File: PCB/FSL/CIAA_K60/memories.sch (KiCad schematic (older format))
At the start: 28 parts, among them J1001 SD CARD, Q1001 FDN340P, U1001 S25FL032P0XMFI013, U1002 24AA1025, U1003 24AA025E48

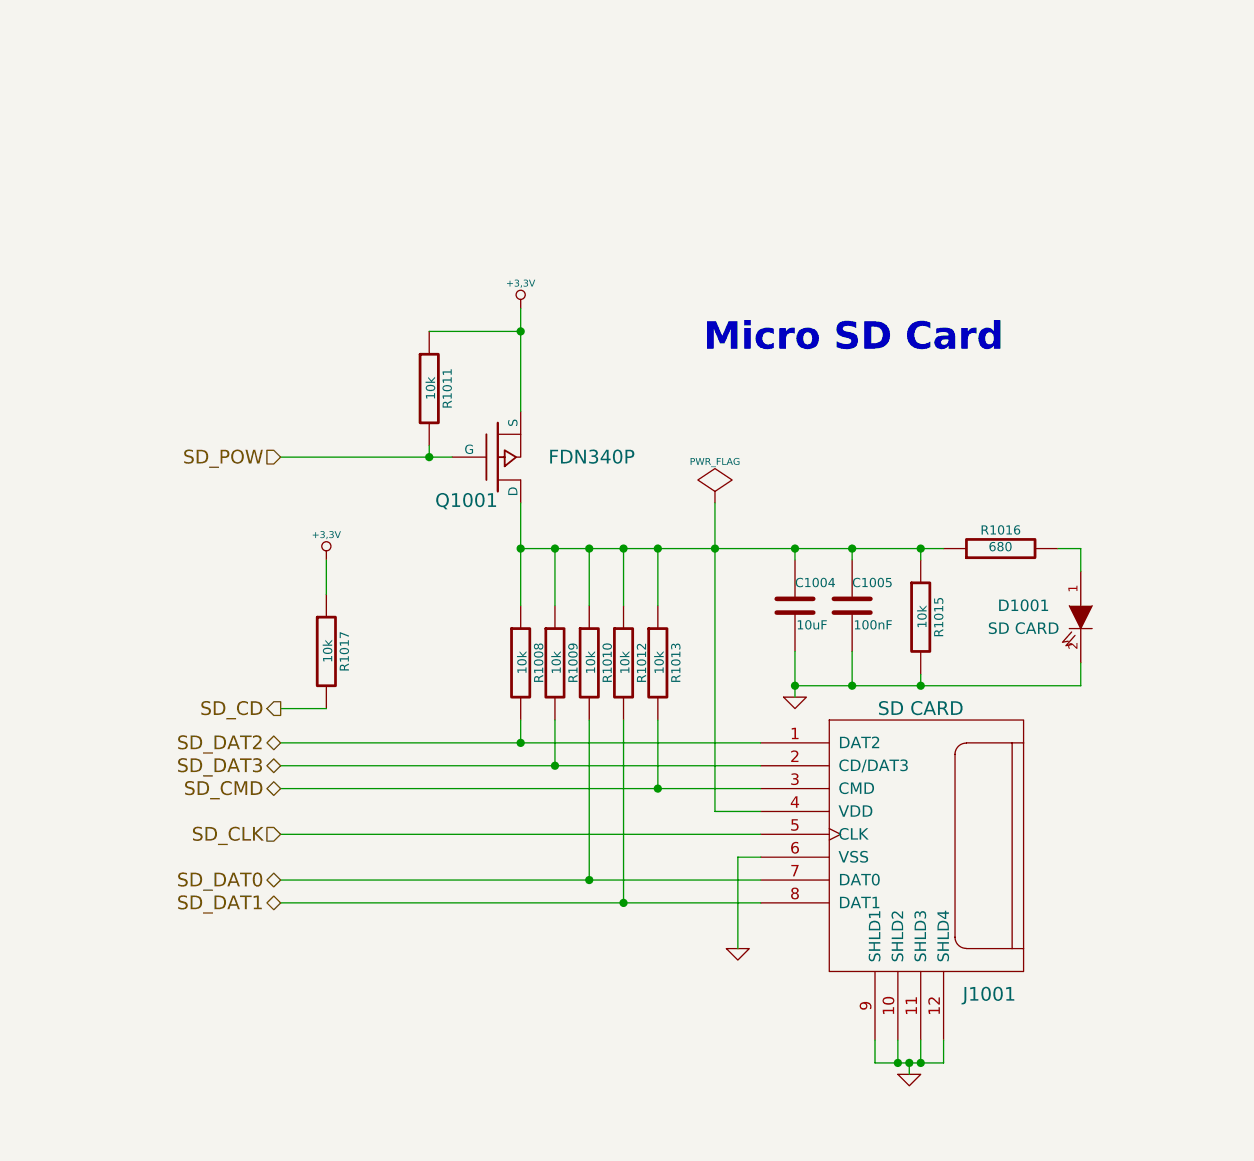
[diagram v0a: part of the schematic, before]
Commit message: Actualizacion de esquematicos. Circuito impreso y modelos 3D
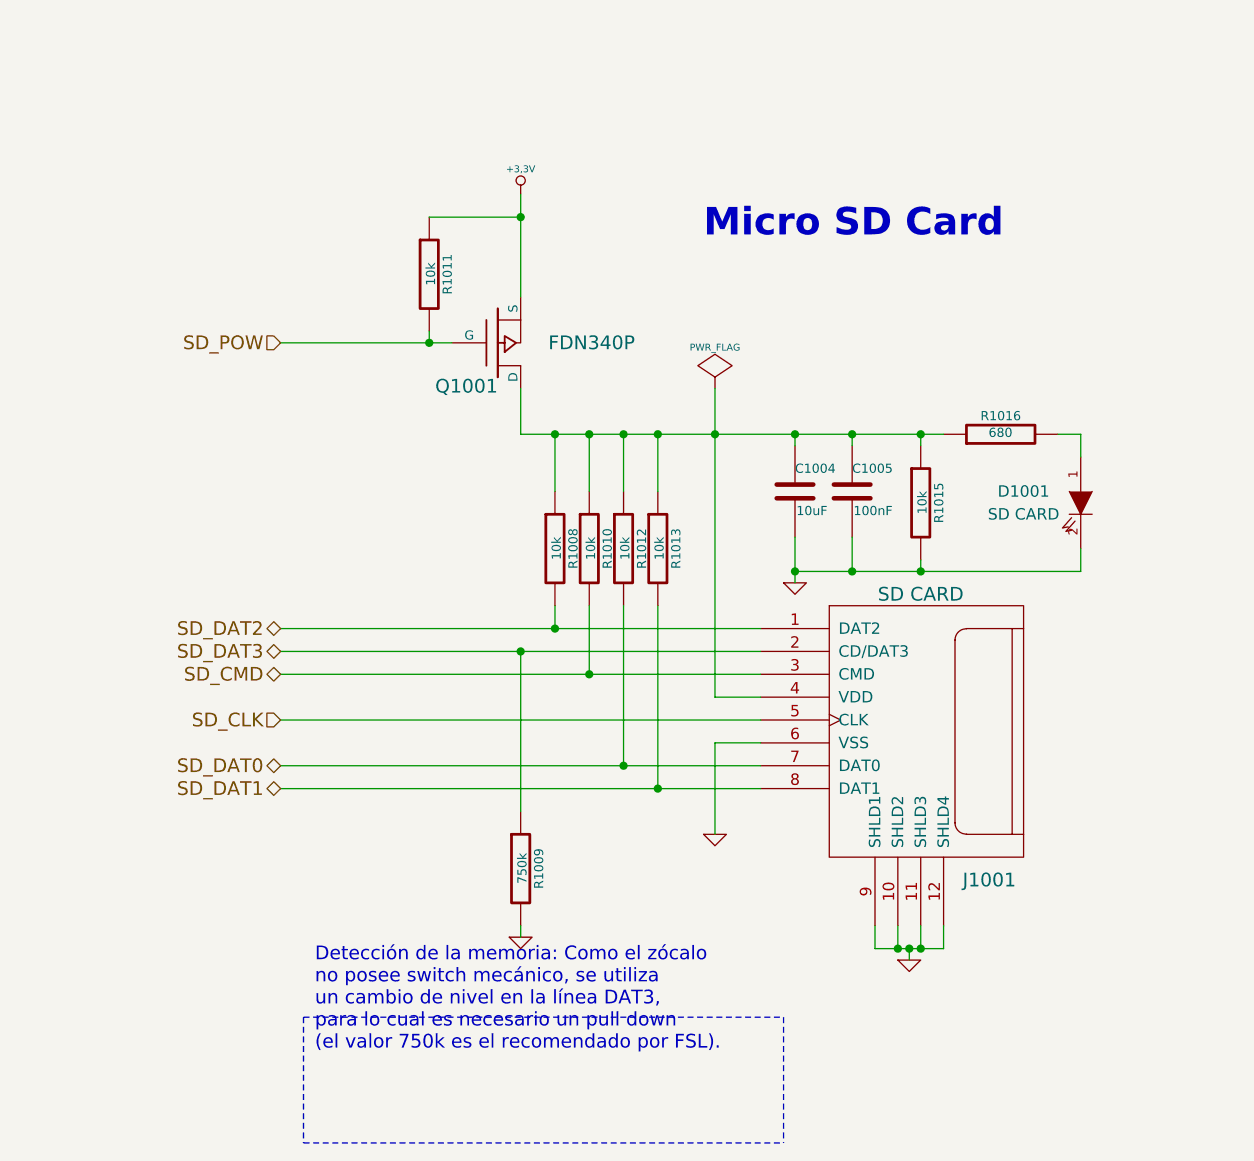
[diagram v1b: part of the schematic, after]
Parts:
- removed R1017: 10k, r_0603, symbol R
- R1009: value 10k -> 750k; Descripcion RES 10K OHM 1/10W 5% 0603 SMD -> RES 750K OHM 1/10W 5% 0603 SMD; Digikey/Mouser 311-10KGRCT-ND -> 311-750KGRCT-ND; Nro. parte RC0603JR-0710KL -> RC0603JR-07750KL
- U1001: footprint SOIC-8 -> SOIC-8_WIDE; Footprint estandar 8-SOIC -> SOIC-8 WIDE
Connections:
- net GND: now also R1009.2
- net SD_CMD: now also R1010.2; no longer R1013.2
- net SD_DAT0: now also R1012.2; no longer R1010.2
- net SD_DAT1: now also R1013.2; no longer R1012.2
- net SD_DAT3: now also R1009.1; no longer R1009.2
- net at C1004.1, C1005.1, J1001.4 (VDD)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: no longer R1009.1
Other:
- note added: "Detección de la memoria: Como el zócalo \nno posee switch mecánico, se utiliza \nun cambio de nivel en la línea DAT3,\npara lo cual es necesario un pull down\n(el valor 750k es el recomendado por FSL)."
- moved on the sheet: C1004, C1005, D1001, J1001, Q1001, R1008, R1010, R1011, R1012, R1013, R1015, R1016

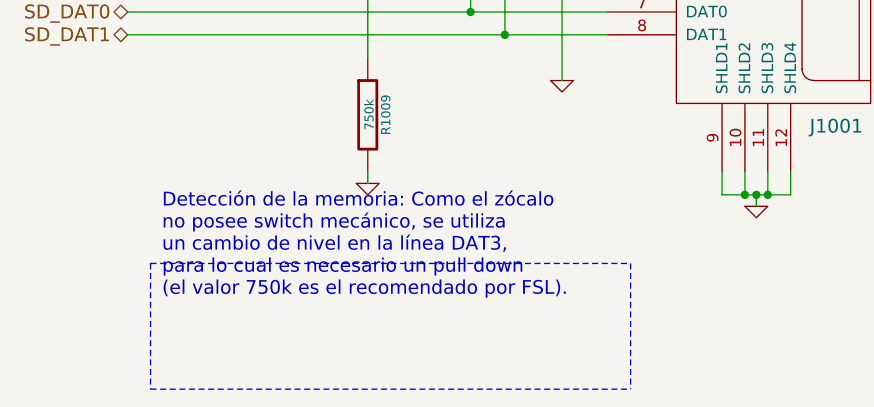
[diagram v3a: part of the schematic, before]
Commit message: Sch files adapted to new eeschema. Fixing some text locations.
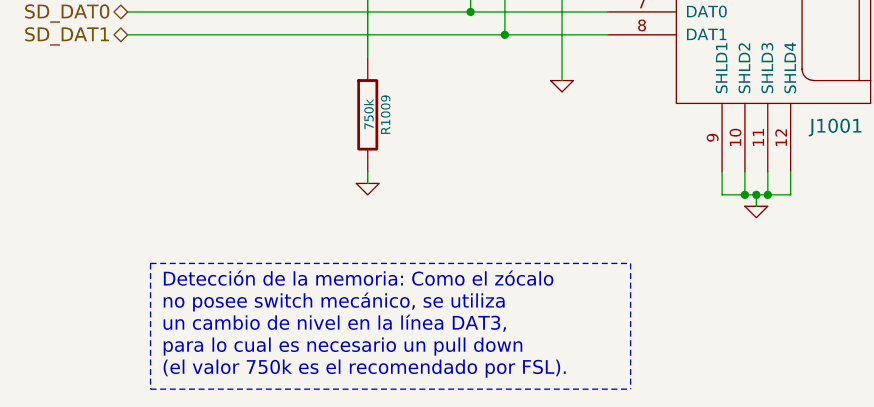
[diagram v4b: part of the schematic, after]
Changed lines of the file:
@@
 EESchema Schematic File Version 2
 LIBS:CIAAK60LIB
-EELAYER 27 0
+LIBS:CIAA_K60-cache
+EELAYER 25 0
 EELAYER END
 $Descr A4 11693 8268
@@
 	1    0    0    -1
 $EndComp
-Text Notes 2000 7250 0    60   ~ 0
+Text Notes 2000 7600 0    60   ~ 0
 Detección de la memoria: Como el zócalo \nno posee switch mecánico, se utiliza \nun cambio de nivel en la línea DAT3,\npara lo cual es necesario un pull down\n(el valor 750k es el recomendado por FSL).
 $Comp

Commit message: Renaming symbol field-names in .sch files for KiCost integration.
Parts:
- C1001, C1002, C1003, C1005: Desc (none) -> CAP CER 0,1UF 16V 10% X7R 0603; Descripcion CAP CER 0,1UF 16V 10% X7R 0603 -> (none); Digikey# (none) -> 399-1096-1-ND; Digikey/Mouser 399-1096-1-ND -> (none); Fabricante Kemet -> (none); Manf (none) -> Kemet; Manf# (none) -> C0603C104K4RACTU; Nro. parte C0603C104K4RACTU -> (none)
- C1004: Desc (none) -> CAP TANT 10UF 6.3V 10% 1206; Descripcion CAP TANT 10UF 6.3V 10% 1206 -> (none); Digikey# (none) -> 399-10116-1-ND; Digikey/Mouser 399-10116-1-ND -> (none); Fabricante Kemet -> (none); Manf (none) -> Kemet; Manf# (none) -> T491A106K006AT7280; Nro. parte T491A106K006AT7280 -> (none)
- D1001: Desc (none) -> LED GRN WATER CLEAR 0603 SMD; Descripcion LED GRN WATER CLEAR 0603 SMD -> (none); Digikey# (none) -> 1080-1399-1-ND; Digikey/Mouser 1080-1399-1-ND -> (none); Fabricante Everlight Electronics Co Ltd -> (none); Manf (none) -> Everlight Electronics Co Ltd; Manf# (none) -> QTLP600C4TR; Nro. parte QTLP600C4TR -> (none)
- J1001: Desc (none) -> CONN MEMORY CARD R/A 8POS SMD; Descripcion CONN MEMORY CARD R/A 8POS SMD -> (none); Digikey# (none) -> WM6698CT-ND; Digikey/Mouser WM6698CT-ND -> (none); Fabricante Molex Inc. -> (none); Manf (none) -> Molex Inc.; Manf# (none) -> 0472192001; Nro. parte 0472192001 -> (none)
- Q1001: Desc (none) -> MOSFET P-CH 20V 2A SSOT3; Descripcion MOSFET P-CH 20V 2A SSOT3 -> (none); Digikey# (none) -> FDN340PCT-ND; Digikey/Mouser FDN340PCT-ND -> (none); Fabricante ON Semiconductor -> (none); Manf (none) -> ON Semiconductor; Manf# (none) -> FDN340P; Nro. parte FDN340P -> (none)
- R1001, R1002, R1003, R1004, R1005, R1006, R1007, R1014: Desc (none) -> RES 0.0 OHM 1/10W JUMP 0603 SMD; Descripcion RES 0.0 OHM 1/10W JUMP 0603 SMD -> (none); Digikey# (none) -> 311-0.0GRCT-ND; Digikey/Mouser 311-0.0GRCT-ND -> (none); Fabricante Yageo -> (none); Manf (none) -> Yageo; Manf# (none) -> RC0603JR-070RL; Nro. parte RC0603JR-070RL -> (none)
- R1008, R1010, R1011, R1012, R1013, R1015: Desc (none) -> RES 10K OHM 1/10W 5% 0603 SMD; Descripcion RES 10K OHM 1/10W 5% 0603 SMD -> (none); Digikey# (none) -> 311-10KGRCT-ND; Digikey/Mouser 311-10KGRCT-ND -> (none); Fabricante Yageo -> (none); Manf (none) -> Yageo; Manf# (none) -> RC0603JR-0710KL; Nro. parte RC0603JR-0710KL -> (none)
- R1009: Desc (none) -> RES 750K OHM 1/10W 5% 0603 SMD; Descripcion RES 750K OHM 1/10W 5% 0603 SMD -> (none); Digikey# (none) -> 311-750KGRCT-ND; Digikey/Mouser 311-750KGRCT-ND -> (none); Fabricante Yageo -> (none); Manf (none) -> Yageo; Manf# (none) -> RC0603JR-07750KL; Nro. parte RC0603JR-07750KL -> (none)
- R1016: Desc (none) -> RES 680 OHM 1/10W 5% 0603 SMD; Descripcion RES 680 OHM 1/10W 5% 0603 SMD -> (none); Digikey# (none) -> 311-680GRCT-ND; Digikey/Mouser 311-680GRCT-ND -> (none); Fabricante Yageo -> (none); Manf (none) -> Yageo; Manf# (none) -> RC0603JR-07680RL; Nro. parte RC0603JR-07680RL -> (none)
- U1001: Desc (none) -> IC NOR FLASH 32MBIT 104MHZ; Descripcion IC NOR FLASH 32MBIT 104MHZ -> (none); Digikey# (none) -> S25FL032P0XMFI013-ND; Digikey/Mouser S25FL032P0XMFI013-ND -> (none); Fabricante Spansion Inc. -> (none); Manf (none) -> Spansion Inc.; Manf# (none) -> S25FL032P0XMFI013; Nro. parte S25FL032P0XMFI013 -> (none)
- U1002: Desc (none) -> IC EEPROM 1MBIT 400KHZ 8SOIC; Descripcion IC EEPROM 1MBIT 400KHZ 8SOIC -> (none); Digikey# (none) -> 24AA1025-I/SN-ND; Digikey/Mouser 24AA1025-I/SN-ND -> (none); Fabricante Microchip Technology -> (none); Manf (none) -> Microchip Technology; Manf# (none) -> 24AA1025-I/SN; Nro. parte 24AA1025-I/SN -> (none)
- U1003: Desc (none) -> IC EEPROM 2KBIT 400KHZ 8SOIC; Descripcion IC EEPROM 2KBIT 400KHZ 8SOIC -> (none); Digikey# (none) -> 24AA025E48-I/SN-ND; Digikey/Mouser 24AA025E48-I/SN-ND -> (none); Fabricante Microchip Technology -> (none); Manf (none) -> Microchip Technology; Manf# (none) -> 24AA025E48-I/SN; Nro. parte 24AA025E48-I/SN -> (none)
